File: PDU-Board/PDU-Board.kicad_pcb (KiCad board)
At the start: 2 copper layers, 127 x 55.9 mm, 11 parts, among them J0 Main Feed, J1 Motor-1, J2 Motor-2, J3 Mother Board, U0 VICOR-DC-DC, U1 VICOR-DC-DC

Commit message: PDU Board work
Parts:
- removed 30A1: Fuse, Vicor:30a Fuse
- removed REF** (x4): , Vicor:Mountingpoint
- removed U0: VICOR-DC-DC, Vicor:Vicor-DCDC-Q
- added F1: 30a, Fuse:Fuse_1206_3216Metric, F.Cu at (113.3, 135.3)
- added U2: VICOR-DC-DC, Vicor:VICOR_VIA_DCM3414, F.Cu at (165.2, 130.1)
- added U3: VICOR-DC-DC, Vicor:VICOR_VIA_DCM3414, F.Cu at (57.1, 130.1)
- added U4: VICOR-DC-DC, Vicor:VICOR_VIA_DCM3414, F.Cu at (93.2, 130.1)
- U1: footprint Vicor:Vicor-DCDC-Q -> Vicor:VICOR_VIA_DCM3414; moved to F.Cu
- moved J2 100.0 mm to (204.2, 52.1), turned to 0 degrees
- moved J3 86.5 mm to (220.6, 52.1)
- moved U1 82.8 mm to (129.1, 130.1)
- moved J1 66.4 mm to (187.8, 60.2)
- moved J0 26.2 mm to (187.8, 52.1), turned to 0 degrees
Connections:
- net 12v-Gnd renamed GND
- J0 pad 2: 48v-Gnd -> 48v_GND
- J1 pad 1: 12v -> +12V
- J2 pad 1: 12v -> +12V
- J3 pad 1: 12v -> +12V
- U1 pad 1: 48v -> +48V
- U1 pad 2: 48v-Gnd -> 48v_GND
- U1 pad 3: 48v-Gnd -> +12V
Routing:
- net GND: track 161.8 -> 0.00 mm
- net 12v: track 156.8 -> 0.00 mm
- net 48v-Gnd: track 81.3 -> 0.00 mm
- net 48v: track 41.7 -> 0.00 mm
- net Net-(F1-Pad2): track 17.5 -> 0.00 mm
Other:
- board outline removed

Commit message: Begun PDU layout
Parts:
- removed F1: 30a, Fuse:Fuse_1206_3216Metric
- moved J1 139.9 mm to (94.0, 164.0), turned to 90 degrees
- moved J2 133.0 mm to (276.0, 164.0), turned to 90 degrees
- moved U1 129.9 mm to (252.0, 88.0), turned to 180 degrees
- moved J3 118.7 mm to (181.0, 164.0)
- moved U3 107.5 mm to (156.0, 88.0), turned to 180 degrees
- moved U2 64.4 mm to (214.0, 88.0), turned to 180 degrees
- moved U4 48.8 mm to (118.0, 88.0), turned to 180 degrees
- moved J0 38.5 mm to (181.0, 90.0)
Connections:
- J0 pad 1: Net-(F1-Pad2) -> +48V
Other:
- board outline added: 210 x 93 mm

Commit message: Finalzed Boards ready for production
YEah
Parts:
- added J4: RJ45, Connectors:RJ45_8, F.Cu at (181.0, 134.6)
- added MH1: MountingHole, Blue_ESC:MountingHole_3mm_custom, F.Cu at (84.0, 84.0)
- added MH2: MountingHole, Blue_ESC:MountingHole_3mm_custom, F.Cu at (286.0, 84.0)
- added MH3: MountingHole, Blue_ESC:MountingHole_3mm_custom, F.Cu at (286.0, 169.0)
- added MH4: MountingHole, Blue_ESC:MountingHole_3mm_custom, F.Cu at (84.0, 169.0)
- added U5: ESC:TMP235A2DBZT, TO_SOT_Packages_SMD:SOT-23, B.Cu at (235.0, 134.6)
- added U6: ESC:TMP235A2DBZT, TO_SOT_Packages_SMD:SOT-23, B.Cu at (135.0, 134.6)
- moved J1 30.1 mm to (88.0, 134.6)
- moved J2 30.1 mm to (282.0, 134.6)
- moved U1 4.00 mm to (256.0, 88.0)
- moved U4 4.00 mm to (114.0, 88.0)
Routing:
- net +3V3: track 0.00 -> 111.7 mm
- net Ext_Temp_0: track 0.00 -> 59.7 mm
- net Ext_Temp_1: track 0.00 -> 52.0 mm
- added copper zone on F.Cu, net +12V
- added copper zone on F.Cu, net +48V
- added copper zone on B.Cu, net 48v_GND
- added copper zone on B.Cu, net GND
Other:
- board text added: "Airzona State Underwater Robotics PDU"
- board text added: "DONT ADD WATER"

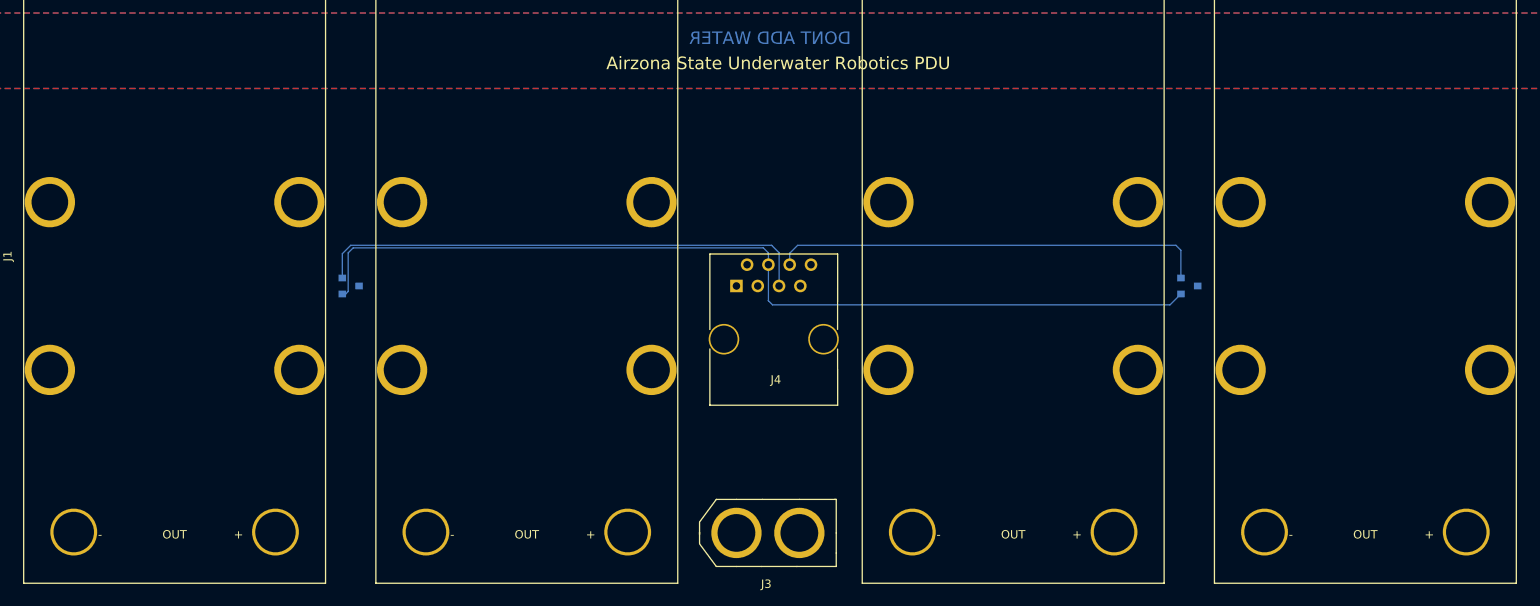
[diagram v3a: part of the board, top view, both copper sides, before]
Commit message: Fixed PDU footprint isuess
vicor foot print fixed
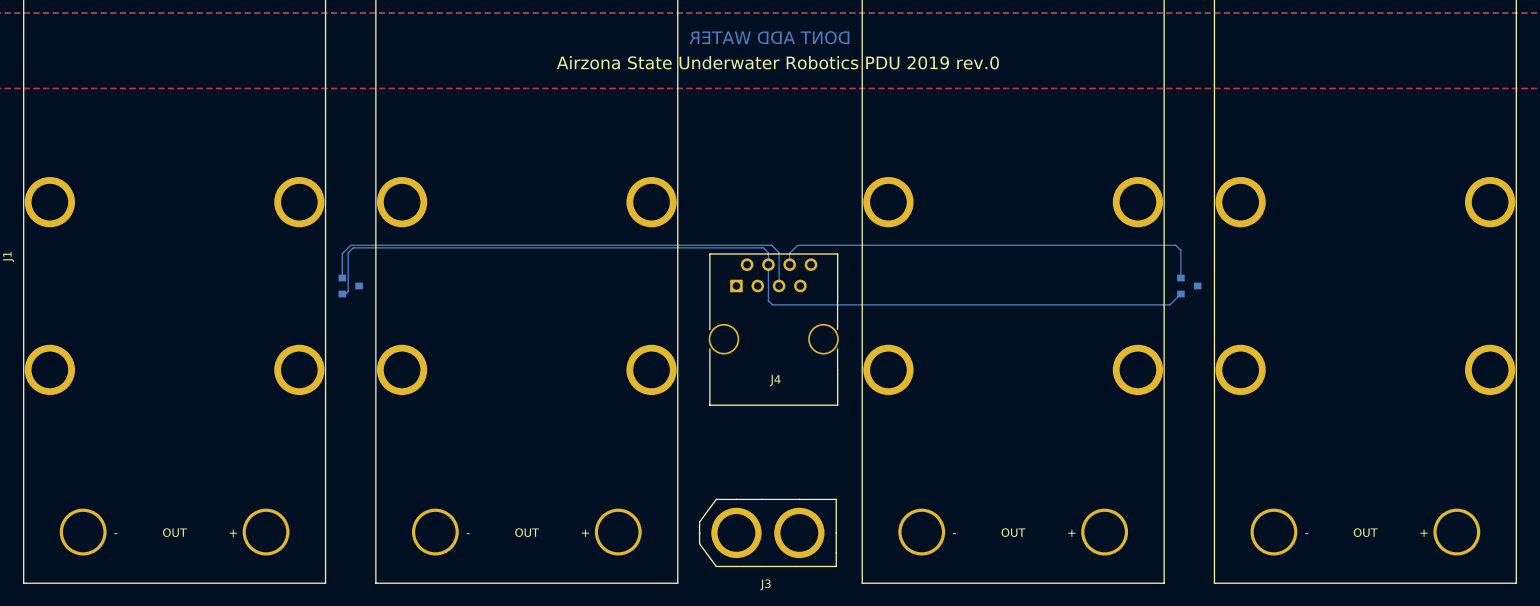
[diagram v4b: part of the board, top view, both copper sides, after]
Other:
- board text added: "Airzona State Underwater Robotics PDU 2019 rev.0"
- board text removed: "Airzona State Underwater Robotics PDU"

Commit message: Re designed PDU pre mec spec
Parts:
- removed MH1, MH2, MH3, MH4: MountingHole, Blue_ESC:MountingHole_3mm_custom
- added J5: RJ45, Connectors:RJ45_8, F.Cu at (180.5, 106.0)
- moved J2 103.0 mm to (181.0, 155.0), turned to 0 degrees
- moved J1 93.7 mm to (181.0, 146.0), turned to 0 degrees
- moved J4 9.06 mm to (180.5, 125.5)
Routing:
- net +3V3: track 111.7 -> 135.5 mm
- net Net-(J4-Pad1): track 0.00 -> 20.1 mm
- net Net-(J4-Pad2): track 0.00 -> 19.5 mm
- net GND: track 0.00 -> 19.5 mm
- net Ext_Temp_1: track 52.0 -> 70.4 mm
- net Ext_Temp_0: track 59.7 -> 75.1 mm
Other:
- board size 210 x 93 mm -> 180 x 93 mm
